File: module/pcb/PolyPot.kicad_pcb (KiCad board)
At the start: 2 copper layers, 50 x 50 mm, 40 parts, among them J1 V_BAT_1S, J10 I2C_TEST, J2 PROG/DEBUG, J3 HUMIDITY_CONN, J4 TOF_DIST_SENS, J5 M3, J6 M3, J7 M3, J8 M3, J9 LUMINOSITY_CONN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

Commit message: PCB: ground connection vias
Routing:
- net GND: track 16.1 -> 113.6 mm, vias 9 -> 29
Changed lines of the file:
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@@
     (thickness 1.6)
     (drawings 39)
-    (tracks 250)
+    (tracks 307)
     (zones 0)
     (modules 40)
@@
   )
   (setup
-    (last_trace_width 0.6)
+    (last_trace_width 0.25)
     (user_trace_width 0.3)
     (user_trace_width 0.6)
@@
     (descr "Mounting Hole 3.2mm, no annular, M3")
     (tags "mounting hole 3.2mm no annular m3")
-    (fp_text reference J8 (at 0 -3.5) (layer F.SilkS) hide
+    (fp_text reference J8 (at 0 -1.5) (layer F.SilkS) hide
       (effects (font (size 1 1) (thickness 0.15)))
     )
@@
     (effects (font (size 1 1) (thickness 0.15)) (justify left mirror))
   )
-  (gr_text 3.3V (at 39.116 41.656 360) (layer B.SilkS)
+  (gr_text 3.3V (at 39.116 41.656) (layer B.SilkS)
     (effects (font (size 1 1) (thickness 0.15)) (justify left mirror))
   )
@@
   (gr_line (start 33.5 80) (end 76.5 80) (layer Edge.Cuts) (width 0.15))
   (gr_line (start 30 33.5) (end 30 76.5) (layer Edge.Cuts) (width 0.15))
+  (segment (start 60 55) (end 58 55) (width 0.25) (layer B.Cu) (net 1))
+  (segment (start 58 55) (end 57 54) (width 0.25) (layer B.Cu) (net 1))
+  (via (at 57 54) (size 1) (drill 0.5) (layers F.Cu B.Cu) (net 1))
+  (segment (start 67 39.5) (end 72 44.5) (width 0.25) (layer F.Cu) (net 1))
+  (via (at 72.5 44.5) (size 1) (drill 0.5) (layers F.Cu B.Cu) (net 1))
+  (segment (start 72 44.5) (end 72.5 44.5) (width 0.25) (layer F.Cu) (net 1))
+  (segment (start 61.5 45.5) (end 55.5 45.5) (width 0.25) (layer B.Cu) (net 1))
+  (via (at 55.5 45.5) (size 1) (drill 0.5) (layers F.Cu B.Cu) (net 1))
+  (segment (start 67 39.5) (end 67 41.415002) (width 0.25) (layer F.Cu) (net 1))
+  (segment (start 67 41.415002) (end 62.915002 45.5) (width 0.25) (layer F.Cu) (net 1))
+  (segment (start 62.915002 45.5) (end 61.5 45.5) (width 0.25) (layer F.Cu) (net 1))
+  (via (at 61.5 45.5) (size 1) (drill 0.5) (layers F.Cu B.Cu) (net 1))
+  (segment (start 66.5 75.5) (end 72 75.5) (width 0.25) (layer F.Cu) (net 1))
+  (via (at 72 75.5) (size 1) (drill 0.5) (layers F.Cu B.Cu) (net 1))
+  (segment (start 71 66) (end 71 71) (width 0.25) (layer B.Cu) (net 1))
+  (segment (start 71 71) (end 66.5 75.5) (width 0.25) (layer B.Cu) (net 1))
+  (via (at 66.5 75.5) (size 1) (drill 0.5) (layers F.Cu B.Cu) (net 1))
+  (segment (start 38 36.05) (end 33.45 36.05) (width 0.25) (layer F.Cu) (net 1))
+  (segment (start 33.45 36.05) (end 32 37.5) (width 0.25) (layer F.Cu) (net 1))
+  (via (at 32 37.5) (size 1) (drill 0.5) (layers F.Cu B.Cu) (net 1))
+  (segment (start 44.085 54.3) (end 44.085 56.915) (width 0.25) (layer F.Cu) (net 1))
+  (segment (start 44.085 56.915) (end 44 57) (width 0.25) (layer F.Cu) (net 1))
+  (via (at 44 57) (size 1) (drill 0.5) (layers F.Cu B.Cu) (net 1))
+  (segment (start 71 66) (end 65.5 66) (width 0.25) (layer B.Cu) (net 1))
+  (via (at 65.5 66) (size 1) (drill 0.5) (layers F.Cu B.Cu) (net 1))
+  (segment (start 77 70.08) (end 75.08 70.08) (width 0.25) (layer F.Cu) (net 1))
+  (segment (start 75.08 70.08) (end 71 66) (width 0.25) (layer F.Cu) (net 1))
+  (via (at 71 66) (size 1) (drill 0.5) (layers F.Cu B.Cu) (net 1))
+  (segment (start 58.8 36.3) (end 56.3 36.3) (width 0.25) (layer F.Cu) (net 1))
+  (segment (start 56.3 36.3) (end 56 36) (width 0.25) (layer F.Cu) (net 1))
+  (segment (start 52 36) (end 56 36) (width 0.25) (layer B.Cu) (net 1))
+  (segment (start 48 36) (end 52 36) (width 0.25) (layer B.Cu) (net 1))
+  (segment (start 44 36) (end 48 36) (width 0.25) (layer B.Cu) (net 1))
+  (via (at 52 36) (size 1) (drill 0.5) (layers F.Cu B.Cu) (net 1))
+  (via (at 48 36) (size 1) (drill 0.5) (layers F.Cu B.Cu) (net 1))
+  (segment (start 40.8 36.3) (end 43.7 36.3) (width 0.25) (layer F.Cu) (net 1))
+  (segment (start 43.7 36.3) (end 44 36) (width 0.25) (layer F.Cu) (net 1))
+  (via (at 44 36) (size 1) (drill 0.5) (layers F.Cu B.Cu) (net 1))
+  (segment (start 31.8 61.5) (end 31.8 64.2) (width 0.25) (layer F.Cu) (net 1))
+  (segment (start 31.8 64.2) (end 31.5 64.5) (width 0.25) (layer F.Cu) (net 1))
+  (via (at 31.5 64.5) (size 1) (drill 0.5) (layers F.Cu B.Cu) (net 1))
+  (via (at 56 36) (size 1) (drill 0.5) (layers F.Cu B.Cu) (net 1))
+  (segment (start 39.8 70.095) (end 39.8 68.7) (width 0.25) (layer F.Cu) (net 1))
+  (segment (start 39.8 68.7) (end 40 68.5) (width 0.25) (layer F.Cu) (net 1))
+  (via (at 40 68.5) (size 1) (drill 0.5) (layers F.Cu B.Cu) (net 1))
+  (segment (start 39.8 73.905) (end 38.095 73.905) (width 0.25) (layer F.Cu) (net 1))
+  (segment (start 38.095 73.905) (end 38 74) (width 0.25) (layer F.Cu) (net 1))
+  (via (at 38 74) (size 1) (drill 0.5) (layers F.Cu B.Cu) (net 1))
+  (segment (start 51.7 67.65) (end 51.35 67.65) (width 0.25) (layer F.Cu) (net 1))
+  (segment (start 51.35 67.65) (end 50 69) (width 0.25) (layer F.Cu) (net 1))
+  (via (at 50 69) (size 1) (drill 0.5) (layers F.Cu B.Cu) (net 1))
+  (segment (start 58.1 56.5) (end 58.25 56.5) (width 0.25) (layer F.Cu) (net 1))
+  (segment (start 58.25 56.5) (end 59.75 55) (width 0.25) (layer F.Cu) (net 1))
+  (segment (start 59.75 55) (end 60 55) (width 0.25) (layer F.Cu) (net 1))
+  (via (at 60 55) (size 1) (drill 0.5) (layers F.Cu B.Cu) (net 1))
+  (segment (start 44.085 54.3) (end 44.085 52.085) (width 0.25) (layer F.Cu) (net 1))
+  (segment (start 44.085 52.085) (end 44 52) (width 0.25) (layer F.Cu) (net 1))
+  (via (at 44 52) (size 1) (drill 0.5) (layers F.Cu B.Cu) (net 1))
   (segment (start 65 33) (end 67 35) (width 0.6) (layer B.Cu) (net 1))
   (segment (start 67 35) (end 67 39.5) (width 0.6) (layer B.Cu) (net 1))
@@
   (segment (start 40.8 36.3) (end 38.25 36.3) (width 0.6) (layer F.Cu) (net 1))
   (segment (start 38.25 36.3) (end 38 36.05) (width 0.6) (layer F.Cu) (net 1))
+  (segment (start 37 38) (end 34.55 38) (width 0.6) (layer F.Cu) (net 2))
+  (segment (start 34.55 38) (end 32.5 40.05) (width 0.6) (layer F.Cu) (net 2))
+  (segment (start 32.5 40.05) (end 32.5 41.5) (width 0.6) (layer F.Cu) (net 2))
   (segment (start 37.6 58) (end 37.6 55) (width 0.25) (layer F.Cu) (net 2))
   (segment (start 37 42.5) (end 39.5 45) (width 0.6) (layer B.Cu) (net 2))
@@
   (segment (start 62.1 39.6) (end 62.5 40) (width 0.25) (layer F.Cu) (net 2))
   (via (at 62.5 40) (size 0.6) (drill 0.3) (layers F.Cu B.Cu) (net 2))
-  (segment (start 32.5 41.5) (end 32.5 40.05) (width 0.6) (layer F.Cu) (net 2))
-  (segment (start 32.5 40.05) (end 34.55 38) (width 0.6) (layer F.Cu) (net 2))
-  (segment (start 34.55 38) (end 36.292894 38) (width 0.6) (layer F.Cu) (net 2))
-  (segment (start 36.292894 38) (end 37 38) (width 0.6) (layer F.Cu) (net 2))
   (segment (start 63.5 70.6) (end 65.85 70.6) (width 0.6) (layer F.Cu) (net 2))
   (segment (start 65.85 70.6) (end 66 70.45) (width 0.6) (layer F.Cu) (net 2))
@@
   (segment (start 33.702081 49.12) (end 32.5 49.12) (width 0.25) (layer F.Cu) (net 7))
   (segment (start 46 56.5) (end 46.875001 57.375001) (width 0.25) (layer F.Cu) (net 8))
-  (segment (start 57.074999 55.235001) (end 58.8 53.51) (width 0.25) (layer F.Cu) (net 8))
-  (segment (start 58.8 53.51) (end 58.8 52.81) (width 0.25) (layer F.Cu) (net 8))
   (segment (start 46.875001 57.375001) (end 56.840001 57.375001) (width 0.25) (layer F.Cu) (net 8))
   (segment (start 56.840001 57.375001) (end 57.074999 57.140003) (width 0.25) (layer F.Cu) (net 8))
-  (segment (start 57.074999 57.140003) (end 57.074999 55.235001) (width 0.25) (layer F.Cu) (net 8))
+  (segment (start 57.074999 57.140003) (end 57.074999 55.725001) (width 0.25) (layer F.Cu) (net 8))
+  (segment (start 57.074999 55.725001) (end 58.8 54) (width 0.25) (layer F.Cu) (net 8))
+  (segment (start 58.8 54) (end 58.8 52.81) (width 0.25) (layer F.Cu) (net 8))
   (segment (start 32.5 51.66) (end 41.16 51.66) (width 0.25) (layer B.Cu) (net 8))
   (segment (start 41.16 51.66) (end 46 56.5) (width 0.25) (layer B.Cu) (net 8))

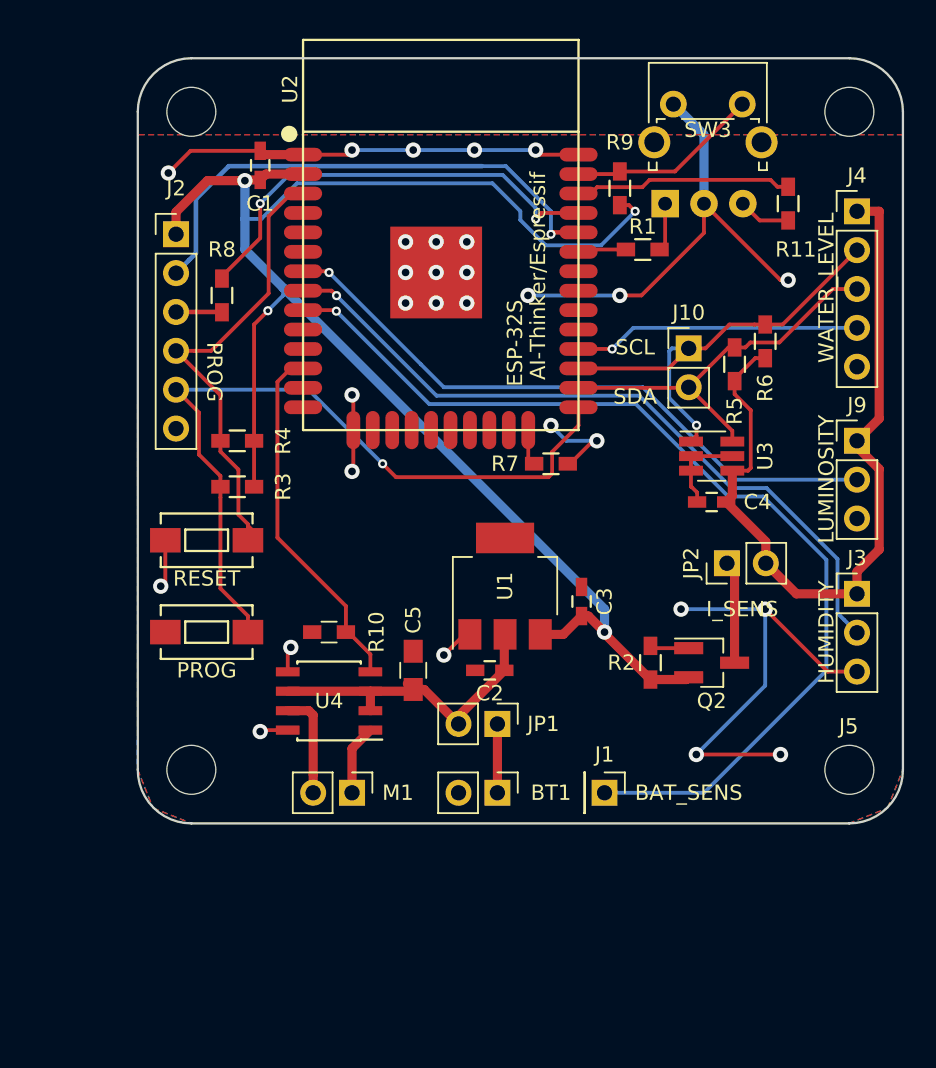
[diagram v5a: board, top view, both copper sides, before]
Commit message: PCB: new routing with luminosity sensor, move LED and button to upper side.
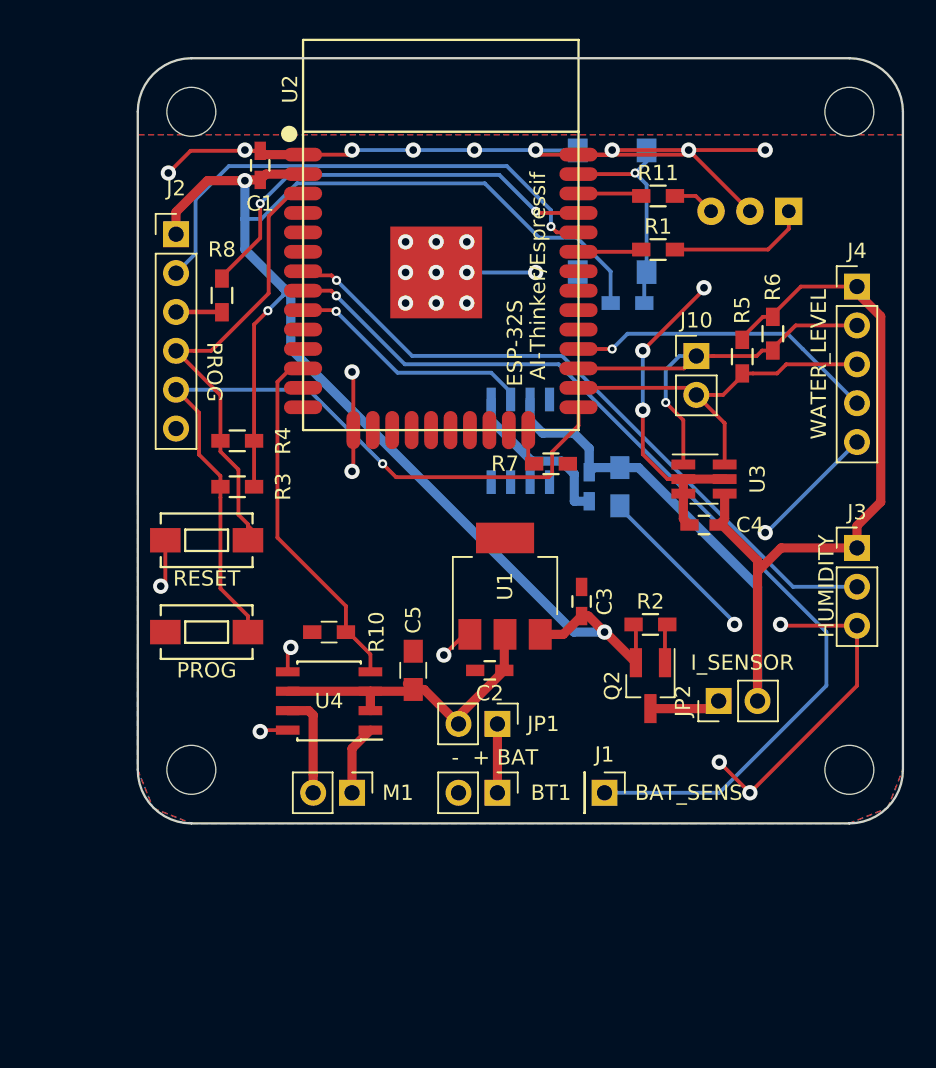
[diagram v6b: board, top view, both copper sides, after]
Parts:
- removed J9: LUMINOSITY_CONN, Pin_Headers:Pin_Header_Straight_1x03_Pitch2.54mm
- added C6: 1uF, Capacitors_SMD:C_0805_HandSoldering, B.Cu at (61.5, 58.0)
- added C7: 100nF, Capacitors_SMD:C_0603_HandSoldering, B.Cu at (59.5, 58.0)
- added U5: MLX75305, Housings_SOIC:SOIC-8_3.9x4.9mm_Pitch1.27mm, B.Cu at (55.0, 55.0)
- R9: moved to B.Cu
- SW3: footprint Buttons_Switches_THT:SW_Tactile_SPST_Angled_PTS645Vx83-2LFS -> Buttons_Switches_SMD:SW_SPST_PTS645; moved to B.Cu
- moved G*** 15.0 mm to (43.0, 64.0)
- moved JP2 9.02 mm to (68.0, 72.0)
- moved R11 8.51 mm to (64.0, 39.0), turned to 180 degrees
- moved D1 8.10 mm to (72.5, 40.0), turned to 180 degrees
- moved SW3 8.06 mm to (61.0, 40.0), turned to 270 degrees
- moved R9 7.52 mm to (62.0, 46.0), turned to 0 degrees
- moved J4 4.92 mm to (77.0, 44.9)
- moved Q2 4.27 mm to (63.5, 71.0), turned to 270 degrees
- moved J3 3.00 mm to (77.0, 62.0)
- moved R2 2.50 mm to (63.5, 67.0), turned to 0 degrees
- moved C4 1.58 mm to (67.0, 60.5)
- moved U3 1.58 mm to (67.0, 57.5)
- moved R1 1.00 mm to (64.0, 42.5)
- moved J10 0.71 mm to (66.5, 49.5)
- moved R5 0.71 mm to (69.5, 49.5), turned to 270 degrees
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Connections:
- U2 pad 7: /SENS_LUMINOSITY -> /SENS_HUMIDITY
- U2 pad 8: /SENS_HUMIDITY -> /V_BAT_SENSE
- U2 pad 9: /V_BAT_SENSE -> /SENS_LUMINOSITY
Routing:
- net GND: track 113.6 -> 150.4 mm, vias 29 -> 33
- net /3V3_SENSORS: track 52.9 -> 78.9 mm
- net /SENS_LUMINOSITY: track 41.8 -> 16.3 mm
- net /LED_GREEN: track 14.3 -> 4.17 mm
- net Net-(D1-Pad1): track 3.15 -> 9.15 mm
- net /SENS_HUMIDITY: track 47.5 -> 44.6 mm
- net /I2C_SDA: track 27.0 -> 24.8 mm
- net Net-(JP2-Pad1): track 6.71 -> 4.67 mm
- net /USER_BTN: track 12.6 -> 14.4 mm, vias 0 -> 1
- net /TOF_GPIO0: track 18.8 -> 20.5 mm
- net /V_BAT_SENSE: track 66.1 -> 64.4 mm
- net +3V3: track 106.4 -> 105.0 mm, vias 4 -> 3
- net /I2C_SCL: track 29.8 -> 28.5 mm
- net /LED_RED: track 3.16 -> 4.16 mm
- net Net-(R8-Pad1): track 29.3 -> 28.5 mm
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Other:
- board text added: "- + BAT"
- board text added: "BAT + -"
- board text added: "I_SENSOR"
- board text removed: "BAT+ -"
- board text removed: "I_SENS"
- board text removed: "LUM"
- board text removed: "LUMINOSITY"
- board text removed: "SCL SDA"

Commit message: PCB: add dimension drawings
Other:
- board text added: "ø3.2mm (4x)"
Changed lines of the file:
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@@
     (area 29.924999 29.924999 80.075001 80.075001)
     (thickness 1.6)
-    (drawings 33)
+    (drawings 44)
     (tracks 322)
     (zones 0)
@@
       (outputformat 1)
       (mirror false)
-      (drillshape 1)
+      (drillshape 0)
       (scaleselection 1)
       (outputdirectory ""))
@@
       (xy 2.537506 -1.998036) (xy 2.624365 -1.969028) (xy 2.629112 -1.968986) (xy 2.728785 -1.984134)) (layer B.SilkS) (width 0.01))
   )
+  (gr_text "ø3.2mm\n(4x)" (at 18 71.5) (layer Dwgs.User)
+    (effects (font (size 1.5 1.5) (thickness 0.3)) (justify left))
+  )
+  (gr_line (start 31.5 75) (end 32.5 75.5) (layer Dwgs.User) (width 0.2))
+  (gr_line (start 32.5 75.5) (end 32 74.5) (layer Dwgs.User) (width 0.2))
+  (gr_line (start 28.5 71.5) (end 18 71.5) (layer Dwgs.User) (width 0.2))
+  (gr_line (start 33.5 76.5) (end 28.5 71.5) (layer Dwgs.User) (width 0.2))
+  (dimension 25 (width 0.3) (layer Dwgs.User)
+    (gr_text "25.000 mm" (at 67.5 86.35) (layer Dwgs.User)
+      (effects (font (size 1.5 1.5) (thickness 0.3)))
+    )
+    (feature1 (pts (xy 80 55) (xy 80 87.7)))
+    (feature2 (pts (xy 55 55) (xy 55 87.7)))
+    (crossbar (pts (xy 55 85) (xy 80 85)))
+    (arrow1a (pts (xy 80 85) (xy 78.873496 85.586421)))
+    (arrow1b (pts (xy 80 85) (xy 78.873496 84.413579)))
+    (arrow2a (pts (xy 55 85) (xy 56.126504 85.586421)))
+    (arrow2b (pts (xy 55 85) (xy 56.126504 84.413579)))
+  )
+  (dimension 25 (width 0.3) (layer Dwgs.User)
+    (gr_text "25.000 mm" (at 23.65 42.5 90) (layer Dwgs.User)
+      (effects (font (size 1.5 1.5) (thickness 0.3)))
+    )
+    (feature1 (pts (xy 55 30) (xy 22.3 30)))
+    (feature2 (pts (xy 55 55) (xy 22.3 55)))
+    (crossbar (pts (xy 25 55) (xy 25 30)))
+    (arrow1a (pts (xy 25 30) (xy 25.586421 31.126504)))
+    (arrow1b (pts (xy 25 30) (xy 24.413579 31.126504)))
+    (arrow2a (pts (xy 25 55) (xy 25.586421 53.873496)))
+    (arrow2b (pts (xy 25 55) (xy 24.413579 53.873496)))
+  )
+  (dimension 43 (width 0.3) (layer Dwgs.User)
+    (gr_text "43.000 mm" (at 85.85 55 270) (layer Dwgs.User)
+      (effects (font (size 1.5 1.5) (thickness 0.3)))
+    )
+    (feature1 (pts (xy 76.5 76.5) (xy 87.2 76.5)))
+    (feature2 (pts (xy 76.5 33.5) (xy 87.2 33.5)))
+    (crossbar (pts (xy 84.5 33.5) (xy 84.5 76.5)))
+    (arrow1a (pts (xy 84.5 76.5) (xy 83.913579 75.373496)))
+    (arrow1b (pts (xy 84.5 76.5) (xy 85.086421 75.373496)))
+    (arrow2a (pts (xy 84.5 33.5) (xy 83.913579 34.626504)))
+    (arrow2b (pts (xy 84.5 33.5) (xy 85.086421 34.626504)))
+  )
+  (dimension 50 (width 0.3) (layer Dwgs.User)
+    (gr_text "50.000 mm" (at 55 18.65) (layer Dwgs.User)
+      (effects (font (size 1.5 1.5) (thickness 0.3)))
+    )
+    (feature1 (pts (xy 80 30) (xy 80 17.3)))
+    (feature2 (pts (xy 30 30) (xy 30 17.3)))
+    (crossbar (pts (xy 30 20) (xy 80 20)))
+    (arrow1a (pts (xy 80 20) (xy 78.873496 20.586421)))
+    (arrow1b (pts (xy 80 20) (xy 78.873496 19.413579)))
+    (arrow2a (pts (xy 30 20) (xy 31.126504 20.586421)))
+    (arrow2b (pts (xy 30 20) (xy 31.126504 19.413579)))
+  )
+  (dimension 43 (width 0.3) (layer Dwgs.User)
+    (gr_text "43.000 mm" (at 55 23.65) (layer Dwgs.User)
+      (effects (font (size 1.5 1.5) (thickness 0.3)))
+    )
+    (feature1 (pts (xy 76.5 33.5) (xy 76.5 22.3)))
+    (feature2 (pts (xy 33.5 33.5) (xy 33.5 22.3)))
+    (crossbar (pts (xy 33.5 25) (xy 76.5 25)))
+    (arrow1a (pts (xy 76.5 25) (xy 75.373496 25.586421)))
+    (arrow1b (pts (xy 76.5 25) (xy 75.373496 24.413579)))
+    (arrow2a (pts (xy 33.5 25) (xy 34.626504 25.586421)))
+    (arrow2b (pts (xy 33.5 25) (xy 34.626504 24.413579)))
+  )
+  (dimension 50 (width 0.3) (layer Dwgs.User)
+    (gr_text "50.000 mm" (at 91.35 55 270) (layer Dwgs.User)
+      (effects (font (size 1.5 1.5) (thickness 0.3)))
+    )
+    (feature1 (pts (xy 80 80) (xy 92.7 80)))
+    (feature2 (pts (xy 80 30) (xy 92.7 30)))
+    (crossbar (pts (xy 90 30) (xy 90 80)))
+    (arrow1a (pts (xy 90 80) (xy 89.413579 78.873496)))
+    (arrow1b (pts (xy 90 80) (xy 90.586421 78.873496)))
+    (arrow2a (pts (xy 90 30) (xy 89.413579 31.126504)))
+    (arrow2b (pts (xy 90 30) (xy 90.586421 31.126504)))
+  )
   (gr_text "-  + BAT" (at 50.5 75.692) (layer F.SilkS)
